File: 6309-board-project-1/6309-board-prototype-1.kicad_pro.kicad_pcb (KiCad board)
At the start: 2 copper layers, 35 parts, among them J1 PWR, J2 FTDI, SW1 B3F-1000, U1 63C09, U2 62256, U3 39FS010, U4 16550, U5 74HCT04, U6 74HCT32, U7 74HCT30, X1 12MHz, X2 1.8432 MHz

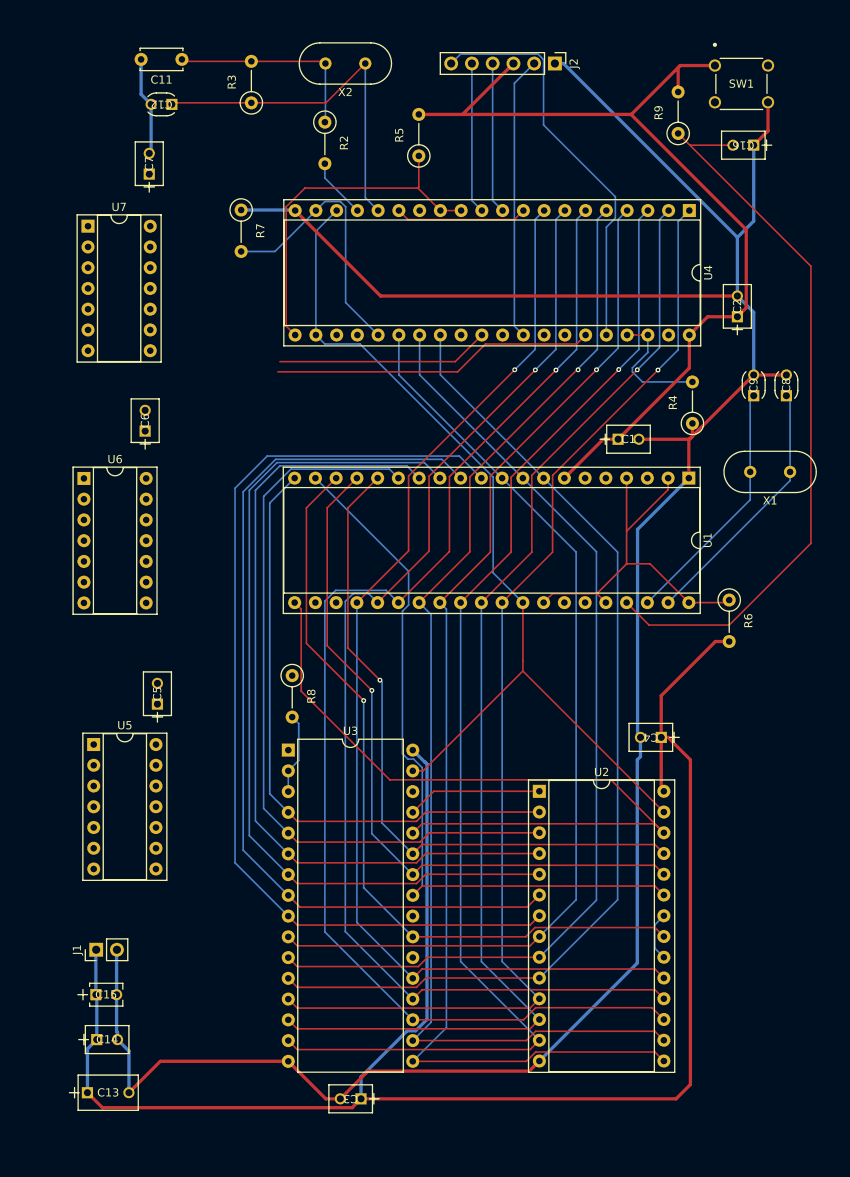
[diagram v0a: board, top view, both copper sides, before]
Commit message: pcb design finished, need to get reviewed
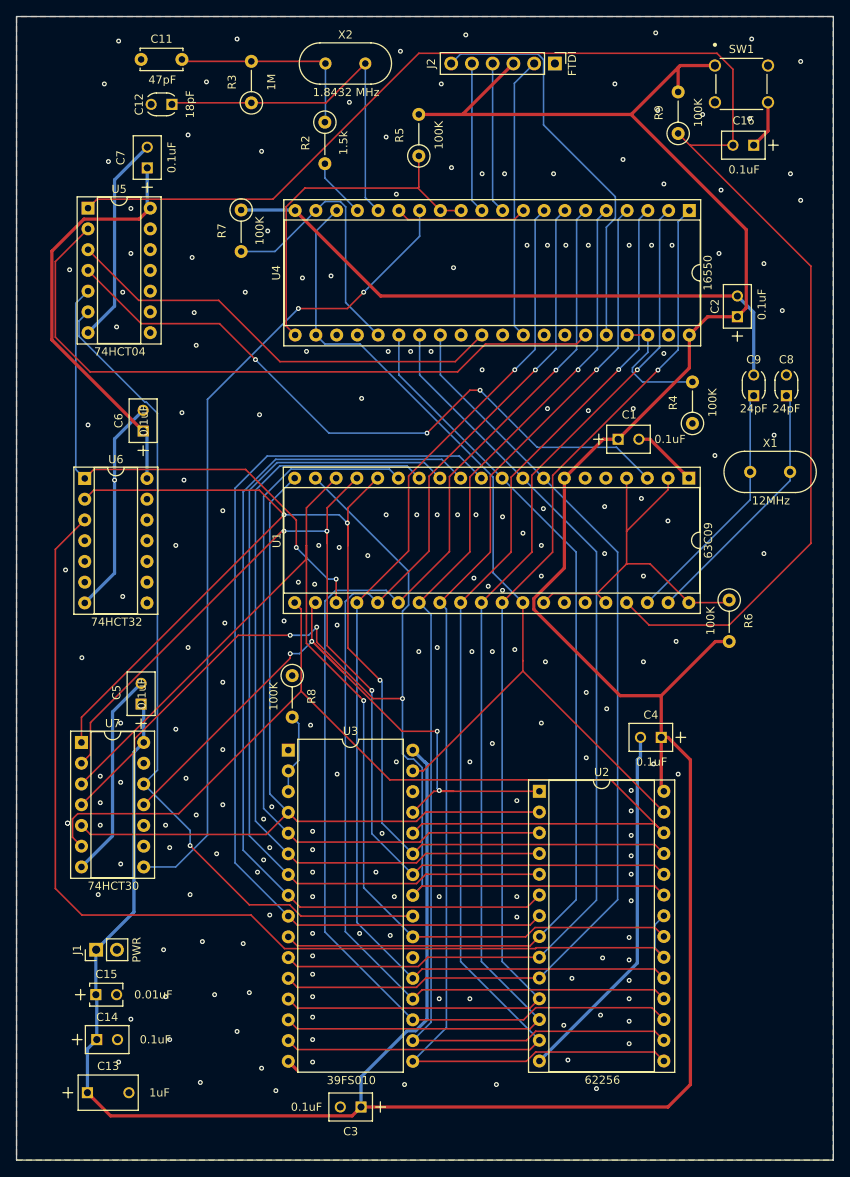
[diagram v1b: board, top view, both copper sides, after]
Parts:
- moved U5 65.7 mm to (35.0, 37.7)
- moved U7 63.2 mm to (34.2, 103.1)
- moved C5 2.00 mm to (41.5, 98.4)
- moved C3 1.00 mm to (68.4, 147.8)
- moved C7 0.80 mm to (42.2, 32.8)
- moved C6 0.25 mm to (41.8, 65.0)
- moved U6 0.10 mm to (34.6, 70.8)
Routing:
- net Net-(U2-~{CS}): track 5.99 -> 130.7 mm
- net +5V: track 322.2 -> 446.2 mm
- net GND: track 325.5 -> 213.7 mm, vias 0 -> 201
- net /!A15: track 0.00 -> 103.8 mm, vias 0 -> 1
- net Net-(U4-~{CS2}): track 0.00 -> 100.2 mm, vias 0 -> 2
- net /!RESET: track 90.0 -> 186.9 mm
- net Net-(U1-~{IRQ}): track 0.00 -> 83.4 mm, vias 0 -> 3
- net /A8: track 82.5 -> 157.7 mm, vias 1 -> 3
- net /A14: track 16.6 -> 85.1 mm, vias 0 -> 4
- net /A15: track 0.00 -> 65.6 mm, vias 0 -> 2
- net /A11: track 89.7 -> 143.6 mm, vias 0 -> 3
- net /A9: track 86.1 -> 131.7 mm, vias 1 -> 3
- net Net-(U4-MR): track 39.5 -> 83.5 mm
- net /A10: track 94.7 -> 135.3 mm
- net /A13: track 94.4 -> 132.7 mm
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- added copper zone on B.Cu, net GND
- added copper zone on F.Cu, net GND
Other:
- board outline added: 100 x 140 mm
- board text added: "0.01uF"
- board text added: "0.1uF"
- board text added: "1.5k"
- board text added: "1.8432 MHz"
- board text added: "100K"
- board text added: "12MHz"
- board text added: "16550"
- board text added: "18pF"
- board text added: "1M"
- board text added: "1uF"
- board text added: "24pF"
- board text added: "39FS010"
- board text added: "47pF"
- board text added: "62256"
- board text added: "63C09"
- board text added: "74HCT04"
- board text added: "74HCT30"
- board text added: "74HCT32"
- board text added: "FTDI"
- board text added: "PWR"

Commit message: generate output files
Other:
- rule pad_to_mask_clearance: 0.0762 -> 0
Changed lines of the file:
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@@
 			(dielectric_constraints no)
 		)
-		(pad_to_mask_clearance 0.0762)
-		(solder_mask_min_width 0.1016)
+		(pad_to_mask_clearance 0)
 		(allow_soldermask_bridges_in_footprints no)
 		(pcbplotparams
-			(layerselection 0x00010fc_ffffffff)
+			(layerselection 0x00010f0_ffffffff)
 			(plot_on_all_layers_selection 0x0000000_00000000)
 			(disableapertmacros no)
@@
 			(outputformat 1)
 			(mirror no)
-			(drillshape 1)
+			(drillshape 0)
 			(scaleselection 1)
-			(outputdirectory "")
+			(outputdirectory "output/")
 		)
 	)
